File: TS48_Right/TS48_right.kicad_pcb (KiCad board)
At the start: 2 copper layers, 124.1 x 77.9 mm, 121 parts, among them Q1 Q_NPN_BCE, SW1 SW_PUSH, U1 ATmega32U4, U2 PRTR5V0U2X, Y1 Crystal_GND2

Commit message: Routing
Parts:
- MX24: value 1U -> MX-1U
- moved R4 1.08 mm to (115.9, 87.8)
- moved R3 0.91 mm to (115.8, 85.7)
- moved R8 0.78 mm to (157.8, 86.9)
- moved R9 0.73 mm to (176.8, 85.1)
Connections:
- U1 pad 20: Net-(U1-Pad20) -> ROW3
- U1 pad 21: Net-(U1-Pad21) -> ROW2
- U1 pad 22: Net-(U1-Pad22) -> ROW1
- U1 pad 25: Net-(U1-Pad25) -> COL4
- U1 pad 26: Net-(U1-Pad26) -> COL3
- U1 pad 27: Net-(U1-Pad27) -> COL2
- U1 pad 28: Net-(U1-Pad28) -> COL1
- U1 pad 31: Net-(U1-Pad31) -> COL0
- U1 pad 41: Net-(U1-Pad41) -> ROW0
- U1 pad 8: Net-(U1-Pad8) -> COL5
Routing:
- net +5V: track 219.1 -> 783.0 mm, vias 2 -> 19
- net LEDGND: track 103.1 -> 598.3 mm, vias 0 -> 17
- net ROW2: track 0.00 -> 170.0 mm, vias 0 -> 14
- net ROW0: track 0.00 -> 163.3 mm, vias 0 -> 16
- net COL0: track 13.5 -> 175.2 mm, vias 0 -> 4
- net ROW3: track 0.00 -> 148.0 mm, vias 0 -> 2
- net ROW1: track 0.00 -> 141.9 mm, vias 0 -> 14
- net COL1: track 15.5 -> 155.1 mm, vias 0 -> 2
- net COL2: track 16.2 -> 131.1 mm, vias 0 -> 2
- net SDA+: track 0.00 -> 101.6 mm, vias 0 -> 3
- net COL5: track 0.00 -> 96.7 mm, vias 0 -> 2
- net SCL-: track 0.00 -> 96.6 mm, vias 0 -> 3
- net COL3: track 0.00 -> 95.9 mm, vias 0 -> 2
- net COL4: track 0.00 -> 86.9 mm, vias 0 -> 2
- net Net-(LED2-Pad2): track 0.00 -> 59.4 mm, vias 0 -> 2
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
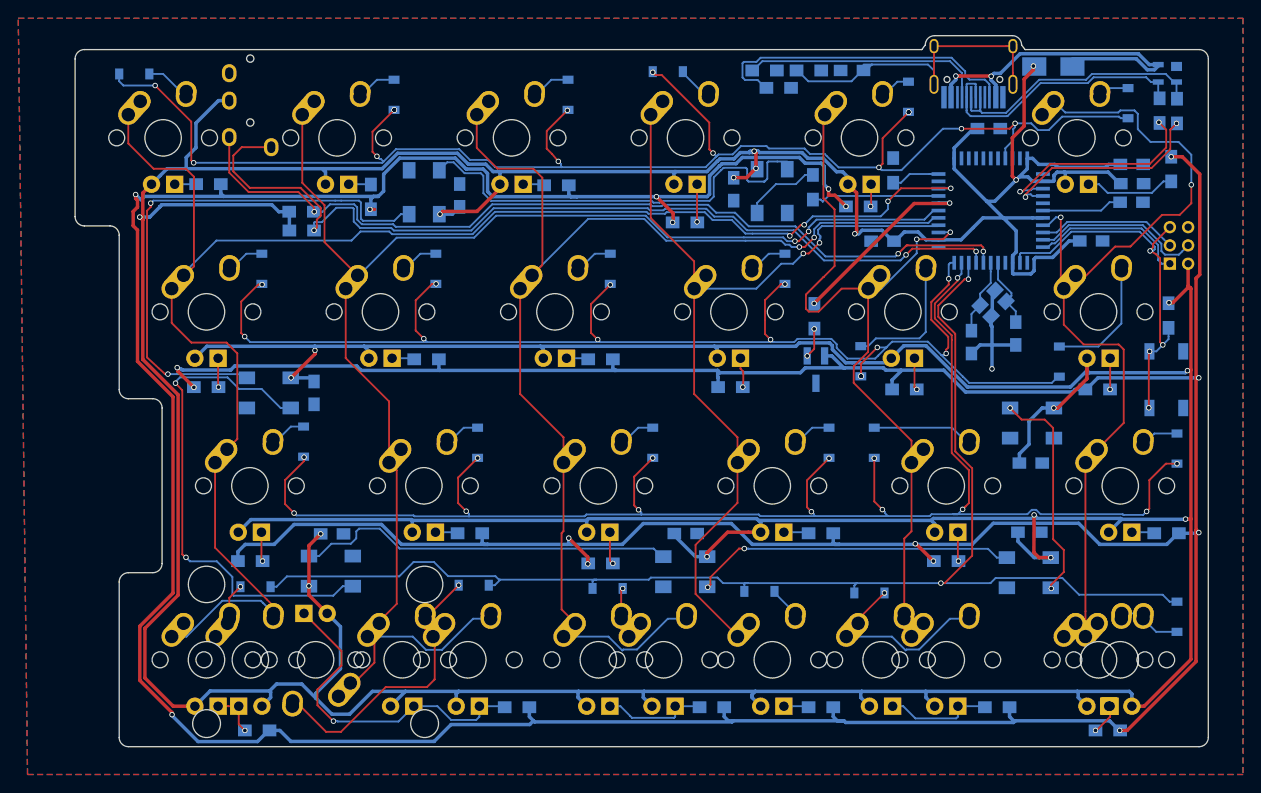
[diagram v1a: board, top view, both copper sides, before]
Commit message: Routed board
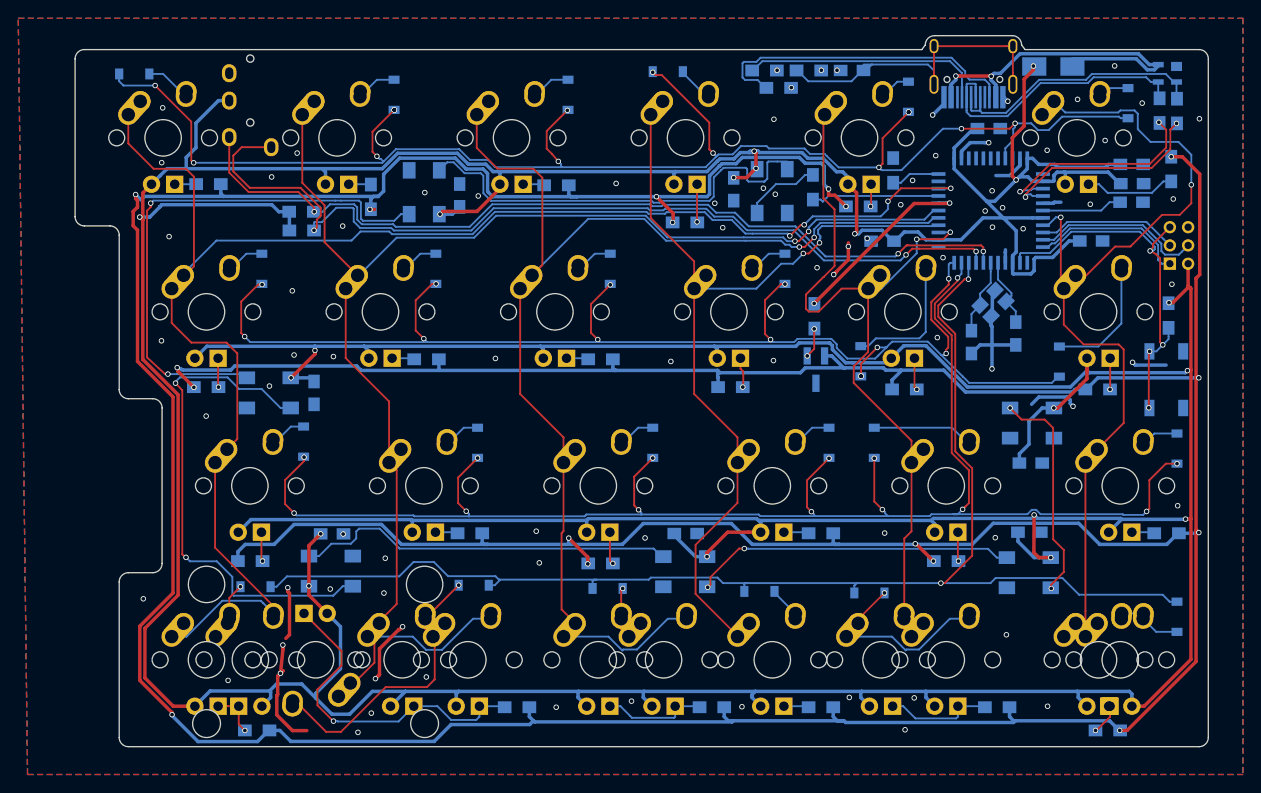
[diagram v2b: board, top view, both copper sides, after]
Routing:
- net GND: track 14.0 -> 68.2 mm, vias 1 -> 84

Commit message: Optimising routing
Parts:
- Y1: value Crystal_GND2 -> (none)
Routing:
- net +5V: track 783.0 -> 791.9 mm
- net GND: track 68.2 -> 73.4 mm, vias 84 -> 83
- net D+: track 23.6 -> 27.2 mm
- net D-: track 23.8 -> 25.5 mm
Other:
- board text added: "JLCJLCJLCJLC"
- board text added: "REV 1.0"

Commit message: Silkscreen
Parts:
- added G***: LOGO, Mixed Lib:Ruslan 48, F.Cu at (165.6, 108.0)
- added REF***: OSHW-Symbol_6.7x6mm_SilkScreen, Symbols:OSHW-Symbol_6.7x6mm_SilkScreen, B.Cu at (156.0, 101.5)
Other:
- board text added: "Github: https://github.com/Gtrx0/TS48"
- board text added: "REV 1.0 Right Side"
- board text removed: "REV 1.0"

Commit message: Gerbers
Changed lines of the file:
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@@
-(kicad_pcb (version 20171130) (host pcbnew "(5.0.0)")
+(kicad_pcb (version 20171130) (host pcbnew "(6.0.0-rc1-dev-1291-g61b749f0b)")
   (general
     (thickness 0.8)
@@
     (zone_45_only no)
     (trace_min 0.2)
-    (segment_width 0.2)
-    (edge_width 0.1)
     (via_size 0.6)
     (via_drill 0.4)
@@
     (uvia_min_size 0.2)
     (uvia_min_drill 0.1)
+    (edge_width 0.1)
+    (segment_width 0.2)
     (pcb_text_width 0.3)
     (pcb_text_size 1.5 1.5)
@@
     (pad_drill 1.04)
     (pad_to_mask_clearance 0.2)
+    (solder_mask_min_width 0.25)
     (aux_axis_origin 0 0)
-    (visible_elements 7FF7F7FF)
+    (visible_elements 7FFFF7FF)
     (pcbplotparams
       (layerselection 0x010fc_ffffffff)
@@
       (usegerberadvancedattributes false)
       (creategerberjobfile false)
-      (excludeedgelayer true)
+      (excludeedgelayer false)
       (linewidth 0.100000)
       (plotframeref false)
       (viasonmask false)
       (mode 1)
-      (useauxorigin false)
+      (useauxorigin true)
       (hpglpennumber 1)
       (hpglpenspeed 20)
@@
       (outputformat 1)
       (mirror false)
-      (drillshape 1)
+      (drillshape 0)
       (scaleselection 1)
-      (outputdirectory ""))
+      (outputdirectory "Gerbers/"))
   )
   (net 0 "")
@@
   (via (at 211.78012 117.89156) (size 0.6) (drill 0.4) (layers F.Cu B.Cu) (net 1))
   (via (at 193.02984 132.01904) (size 0.6) (drill 0.4) (layers F.Cu B.Cu) (net 1))
-  (via (at 181.93512 142.42288) (size 0.6) (drill 0.4) (layers F.Cu B.Cu) (net 1))
+  (via (at 174.43704 142.72768) (size 0.6) (drill 0.4) (layers F.Cu B.Cu) (net 1))
   (via (at 124.87656 127.45212) (size 0.6) (drill 0.4) (layers F.Cu B.Cu) (net 1))
   (via (at 126.91872 131.1402) (size 0.6) (drill 0.4) (layers F.Cu B.Cu) (net 1))
@@
   (via (at 151.98344 139.28852) (size 0.6) (drill 0.4) (layers F.Cu B.Cu) (net 1))
   (via (at 164.07384 139.89812) (size 0.6) (drill 0.4) (layers F.Cu B.Cu) (net 1))
-  (via (at 175.82896 138.88212) (size 0.6) (drill 0.4) (layers F.Cu B.Cu) (net 1))
-  (via (at 182.93588 138.92784) (size 0.6) (drill 0.4) (layers F.Cu B.Cu) (net 1))
+  (via (at 175.83912 139.63396) (size 0.6) (drill 0.4) (layers F.Cu B.Cu) (net 1))
+  (via (at 182.99684 139.55776) (size 0.6) (drill 0.4) (layers F.Cu B.Cu) (net 1))
   (via (at 197.5358 139.84732) (size 0.6) (drill 0.4) (layers F.Cu B.Cu) (net 1))
   (via (at 179.69992 120.88368) (size 0.6) (drill 0.4) (layers F.Cu B.Cu) (net 1))
@@
   (via (at 204.88148 69.73316) (size 0.6) (drill 0.4) (layers F.Cu B.Cu) (net 1))
   (via (at 200.82256 73.39584) (size 0.6) (drill 0.4) (layers F.Cu B.Cu) (net 1))
-  (via (at 197.49008 78.9686) (size 0.6) (drill 0.4) (layers F.Cu B.Cu) (net 1))
+  (via (at 197.50532 78.36408) (size 0.6) (drill 0.4) (layers F.Cu B.Cu) (net 1))
   (via (at 191.09436 78.13548) (size 0.6) (drill 0.4) (layers F.Cu B.Cu) (net 1))
   (via (at 200.32472 107.00512) (size 0.6) (drill 0.4) (layers F.Cu B.Cu) (net 1))
@@
   (segment (start 199.3138 122.7328) (end 198.1454 121.5644) (width 0.204) (layer F.Cu) (net 41))
   (segment (start 198.1454 121.5644) (end 198.1454 109.3724) (width 0.204) (layer F.Cu) (net 41))
-  (segment (start 103.25328 132.21996) (end 107.17703 128.29621) (width 0.204) (layer B.Cu) (net 43))
-  (segment (start 101.63496 132.21996) (end 103.25328 132.21996) (width 0.204) (layer B.Cu) (net 43))
-  (segment (start 107.17703 128.29621) (end 111.40253 128.29621) (width 0.204) (layer B.Cu) (net 43))
-  (segment (start 111.40253 128.29621) (end 111.662181 128.555861) (width 0.204) (layer B.Cu) (net 43))
-  (segment (start 111.662181 128.555861) (end 112.78718 129.68086) (width 0.204) (layer B.Cu) (net 43))
   (segment (start 104.069959 91.684961) (end 101.63496 94.11996) (width 0.204) (layer F.Cu) (net 43))
   (segment (start 104.069959 81.865279) (end 104.069959 91.684961) (width 0.204) (layer F.Cu) (net 43))
@@
   (segment (start 171.818193 86.205167) (end 179.275633 86.205167) (width 0.204) (layer B.Cu) (net 43))
   (segment (start 180.0606 85.4202) (end 180.0606 84.980864) (width 0.204) (layer B.Cu) (net 43))
+  (segment (start 103.25328 132.21996) (end 107.17703 128.29621) (width 0.204) (layer B.Cu) (net 43))
+  (segment (start 101.63496 132.21996) (end 103.25328 132.21996) (width 0.204) (layer B.Cu) (net 43))
+  (segment (start 107.17703 128.29621) (end 111.40253 128.29621) (width 0.204) (layer B.Cu) (net 43))
+  (segment (start 111.40253 128.29621) (end 111.662181 128.555861) (width 0.204) (layer B.Cu) (net 43))
+  (segment (start 111.662181 128.555861) (end 112.78718 129.68086) (width 0.204) (layer B.Cu) (net 43))
   (segment (start 123.40996 82.68996) (end 123.444 82.724) (width 0.204) (layer B.Cu) (net 44))
   (segment (start 121.01696 82.68996) (end 123.40996 82.68996) (width 0.204) (layer B.Cu) (net 44))
@@
   (segment (start 211.6549 71.49342) (end 211.6549 73.2719) (width 0.204) (layer B.Cu) (net 92))
   (segment (start 190.120099 74.642381) (end 190.186981 74.642381) (width 0.204) (layer B.Cu) (net 92))
-  (segment (start 190.120099 74.642381) (end 190.131101 74.642381) (width 0.204) (layer B.Cu) (net 92))
-  (segment (start 190.131101 74.642381) (end 190.36284 74.87412) (width 0.204) (layer B.Cu) (net 92))
-  (segment (start 190.36284 74.87412) (end 192.99428 74.87412) (width 0.204) (layer B.Cu) (net 92))
-  (segment (start 192.99428 74.87412) (end 196.6214 71.247) (width 0.204) (layer B.Cu) (net 92))
   (segment (start 196.6214 71.247) (end 201.75728 71.247) (width 0.204) (layer B.Cu) (net 92))
+  (segment (start 192.99428 74.87412) (end 196.6214 71.247) (width 0.204) (layer B.Cu) (net 92))
+  (segment (start 202.3872 70.61708) (end 210.47856 70.61708) (width 0.204) (layer B.Cu) (net 92))
+  (segment (start 190.36284 74.87412) (end 192.99428 74.87412) (width 0.204) (layer B.Cu) (net 92))
   (segment (start 201.75728 71.247) (end 202.3872 70.61708) (width 0.204) (layer B.Cu) (net 92))
-  (segment (start 211.3549 71.49342) (end 211.6549 71.49342) (width 0.204) (layer B.Cu) (net 92))
+  (segment (start 190.120099 74.642381) (end 190.131101 74.642381) (width 0.204) (layer B.Cu) (net 92))
+  (segment (start 190.131101 74.642381) (end 190.36284 74.87412) (width 0.204) (layer B.Cu) (net 92))
   (segment (start 210.47856 70.61708) (end 211.3549 71.49342) (width 0.204) (layer B.Cu) (net 92))
-  (segment (start 202.3872 70.61708) (end 210.47856 70.61708) (width 0.204) (layer B.Cu) (net 92))
+  (segment (start 211.3549 71.49342) (end 211.6549 71.49342) (width 0.204) (layer B.Cu) (net 92))
   (segment (start 188.6705 71.73398) (end 188.6705 73.16298) (width 0.204) (layer B.Cu) (net 93))
   (segment (start 188.720901 71.683579) (end 188.6705 71.73398) (width 0.204) (layer B.Cu) (net 93))
@@
   (segment (start 209.6549 73.1299) (end 209.804 73.279) (width 0.204) (layer B.Cu) (net 93))
   (segment (start 209.6549 71.49342) (end 209.6549 73.1299) (width 0.204) (layer B.Cu) (net 93))
-  (segment (start 188.6705 74.59198) (end 188.6712 74.59268) (width 0.204) (layer B.Cu) (net 93))
-  (segment (start 188.6705 73.16298) (end 188.6705 74.59198) (width 0.204) (layer B.Cu) (net 93))
-  (segment (start 188.6712 74.59268) (end 188.6712 74.79792) (width 0.204) (layer B.Cu) (net 93))
-  (segment (start 188.6712 74.79792) (end 189.10808 75.2348) (width 0.204) (layer B.Cu) (net 93))
   (segment (start 189.10808 75.2348) (end 193.14668 75.2348) (width 0.204) (layer B.Cu) (net 93))
+  (segment (start 208.8509 71.49342) (end 209.6549 71.49342) (width 0.204) (layer B.Cu) (net 93))
+  (segment (start 188.6712 74.59268) (end 188.6712 74.79792) (width 0.204) (layer B.Cu) (net 93))
   (segment (start 193.14668 75.2348) (end 196.76872 71.61276) (width 0.204) (layer B.Cu) (net 93))
+  (segment (start 188.6705 73.16298) (end 188.6705 74.59198) (width 0.204) (layer B.Cu) (net 93))
+  (segment (start 188.6712 74.79792) (end 189.10808 75.2348) (width 0.204) (layer B.Cu) (net 93))
+  (segment (start 188.6705 74.59198) (end 188.6712 74.59268) (width 0.204) (layer B.Cu) (net 93))
+  (segment (start 208.33524 70.97776) (end 208.8509 71.49342) (width 0.204) (layer B.Cu) (net 93))
   (segment (start 196.76872 71.61276) (end 201.94524 71.61276) (width 0.204) (layer B.Cu) (net 93))
   (segment (start 201.94524 71.61276) (end 202.58024 70.97776) (width 0.204) (layer B.Cu) (net 93))
-  (segment (start 208.8509 71.49342) (end 209.6549 71.49342) (width 0.204) (layer B.Cu) (net 93))
-  (segment (start 208.33524 70.97776) (end 208.8509 71.49342) (width 0.204) (layer B.Cu) (net 93))
   (segment (start 202.58024 70.97776) (end 208.33524 70.97776) (width 0.204) (layer B.Cu) (net 93))
   (segment (start 164.4142 71.2724) (end 165.7874 71.2724) (width 0.204) (layer B.Cu) (net 94))
